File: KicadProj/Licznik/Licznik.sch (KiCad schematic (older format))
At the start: 15 parts, among them J1 RTC Module, J2 7Seg-Display, J3 GND_IN, J4 POWER_IN, J5 +, J7 +, J8 -, J9 +, U1 ATmega328P-PU, Y1 Crystal

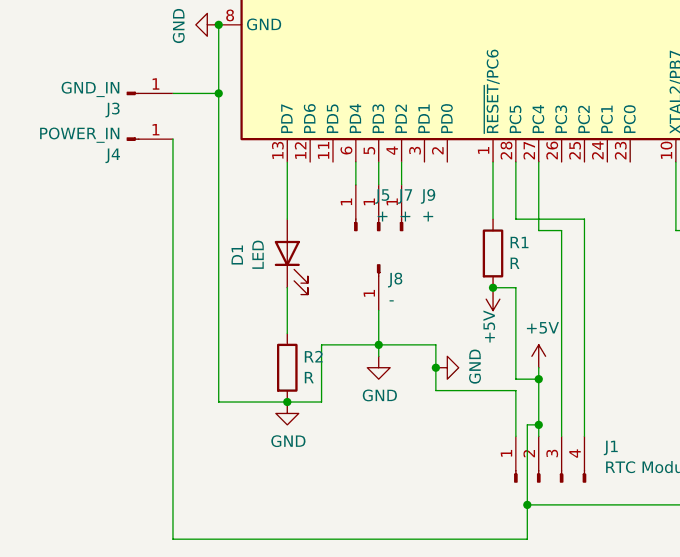
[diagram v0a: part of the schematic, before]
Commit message: created PCB board
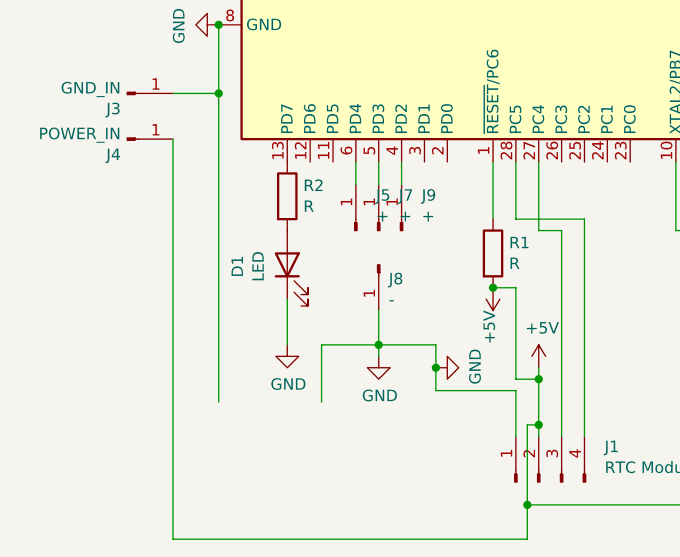
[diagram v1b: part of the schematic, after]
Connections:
- wire segments 66 -> 63
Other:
- moved on the sheet: D1, R2

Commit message: update schematics
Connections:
- wire segments 63 -> 65
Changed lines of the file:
@@
-$EndComp
-$Comp
-L power:GND #PWR013
-U 1 1 60A9E3BD
-P 2700 3100
-F 0 "#PWR013" H 2700 2850 50  0001 C CNN
-F 1 "GND" H 2705 2927 50  0000 C CNN
-F 2 "" H 2700 3100 50  0001 C CNN
-F 3 "" H 2700 3100 50  0001 C CNN
-	1    2700 3100
-	1    0    0    -1
 $EndComp
 $Comp
@@
 	2850 3100 2850 3350
 Wire Wire Line
-	2700 2900 2700 3100
+	2700 2900 2700 3350
+Wire Wire Line
+	2850 3350 2700 3350
+Connection ~ 2700 3350
+Wire Wire Line
+	2400 3350 2700 3350
+$Comp
+L power:GND #PWR013
+U 1 1 60A9E3BD
+P 2700 3350
+F 0 "#PWR013" H 2700 3100 50  0001 C CNN
+F 1 "GND" H 2705 3177 50  0000 C CNN
+F 2 "" H 2700 3350 50  0001 C CNN
+F 3 "" H 2700 3350 50  0001 C CNN
+	1    2700 3350
+	1    0    0    -1
+$EndComp
 $EndSCHEMATC
